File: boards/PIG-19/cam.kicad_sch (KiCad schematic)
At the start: 2 parts, among them J12 Conn_01x02_Pin, U1 ESP32-CAM

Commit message: V1 of PCB
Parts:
- removed J12: Conn_01x02_Pin, Connector_PinHeader_2.54mm:PinHeader_1x02_P2.54mm_Horizontal, symbol Connector:Conn_01x02_Pin
- removed U1: ESP32-CAM, ESP32-CAM:ESP32-CAM, symbol ESP32-CAM:ESP32-CAM
- added USS1: Conn_02x04_Odd_Even, Connector_PinHeader_2.54mm:PinHeader_2x04_P2.54mm_Horizontal, symbol Connector_Generic:Conn_02x04_Odd_Even
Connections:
- net GND: now also USS1.7 (Pin_7), USS1.8 (Pin_8)
- new net +5V: USS1.1 (Pin_1), USS1.2 (Pin_2)
- new net Echo_1: USS1.3 (Pin_3)
- new net Echo_2: USS1.4 (Pin_4)
- new net Trig_1: USS1.5 (Pin_5)
- new net Trig_2: USS1.6 (Pin_6)

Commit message: board updates
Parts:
- USS1: now left out of the parts list
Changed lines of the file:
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@@
 		(unit 1)
 		(exclude_from_sim no)
-		(in_bom yes)
+		(in_bom no)
 		(on_board yes)
 		(dnp no)

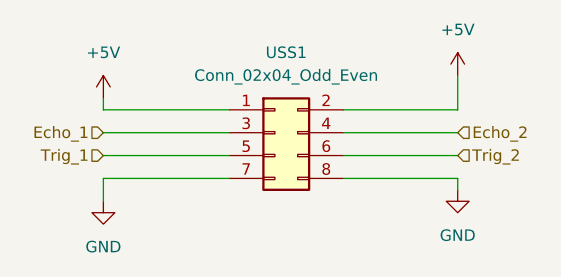
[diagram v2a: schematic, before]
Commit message: Added BOM for main board
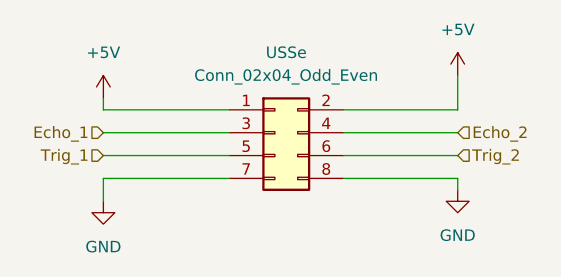
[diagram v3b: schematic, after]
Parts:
- renumbered USS1 to USSe
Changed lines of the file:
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@@
 		(dnp no)
 		(fields_autoplaced yes)
-		(property "Reference" "USS1"
+		(property "Reference" "USSe"
 			(at 100.33 83.82 0)
 			(effects
@@
 			(project "PIG-19"
 				(path "/469e864f-3700-4a04-a1e1-a9f39f3c0d0e/6af7b4d3-4cb5-4844-83f3-c851284dca4a"
-					(reference "USS1")
+					(reference "USSe")
 					(unit 1)
 				)
